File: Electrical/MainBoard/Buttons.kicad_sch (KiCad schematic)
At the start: 6 parts, among them SW4 User_Button, SW5 User_Button, SW6 User_Button

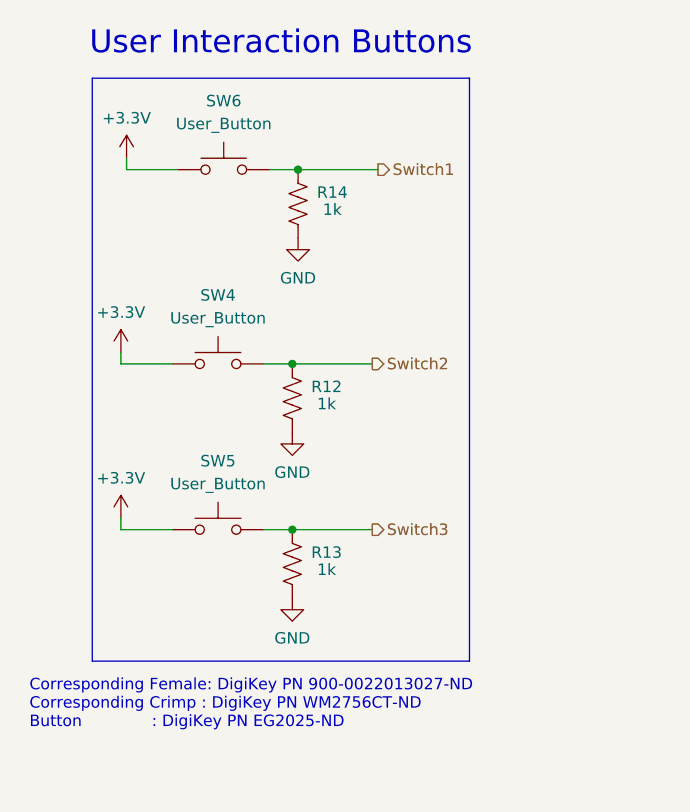
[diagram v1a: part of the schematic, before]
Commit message: Use more molex picoblades and make schematic prettier
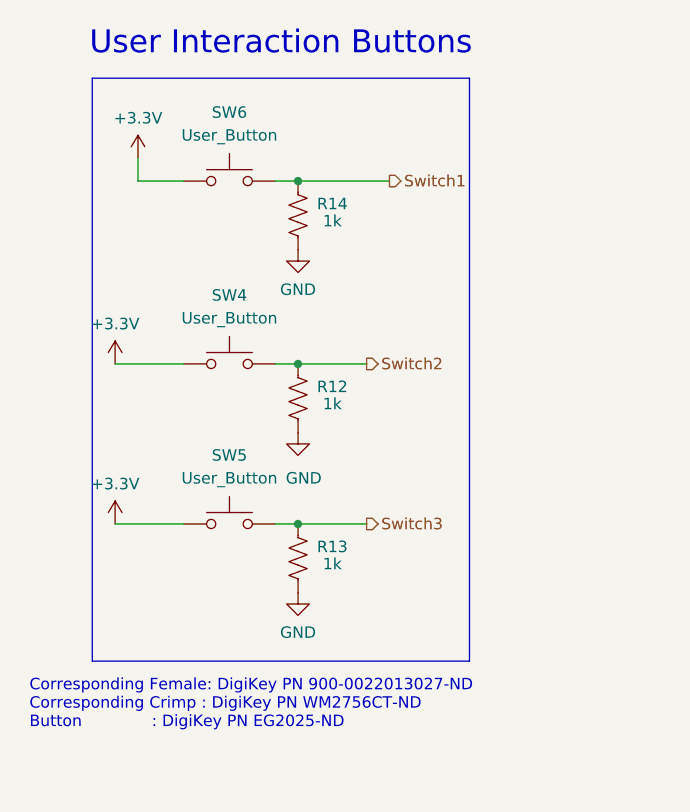
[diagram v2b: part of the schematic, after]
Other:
- moved on the sheet: R12, R13, R14, SW4, SW5, SW6

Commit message: Finalize updated schematics
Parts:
- R12, R13, SW4, SW5: now in the parts list
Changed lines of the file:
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@@
 		(unit 1)
 		(exclude_from_sim no)
-		(in_bom no)
+		(in_bom yes)
 		(on_board yes)
 		(dnp no)
@@
 		(unit 1)
 		(exclude_from_sim no)
-		(in_bom no)
+		(in_bom yes)
 		(on_board yes)
 		(dnp no)
@@
 		(unit 1)
 		(exclude_from_sim no)
-		(in_bom no)
+		(in_bom yes)
 		(on_board yes)
 		(dnp no)
@@
 		(unit 1)
 		(exclude_from_sim no)
-		(in_bom no)
-		(on_board yes)
-		(dnp no)
+		(in_bom yes)
+		(on_board yes)
+		(dnp no)
